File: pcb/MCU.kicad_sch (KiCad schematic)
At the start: 14 parts, among them SW1 SW_Push, SW1 SW_SPDT, U1 STM32F071RBTx, Y1 TG2520SMN_16.0000M-MCGNNM0

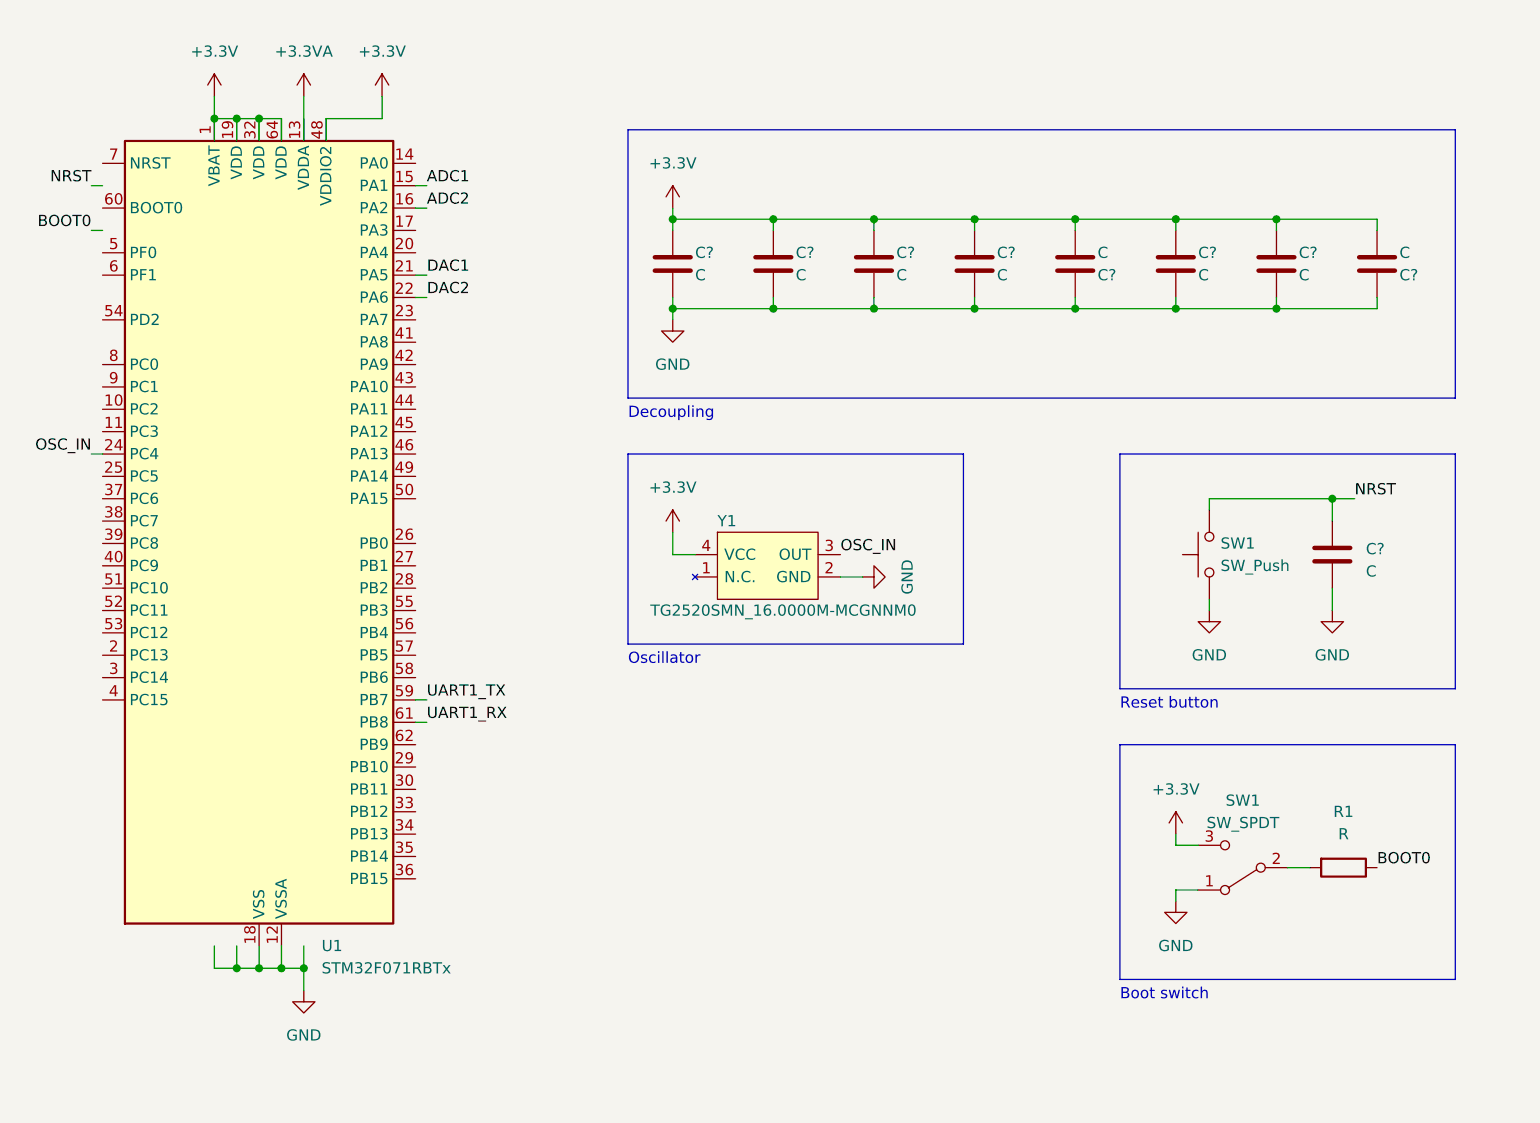
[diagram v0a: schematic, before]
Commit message: Completed schematic oranization and components connection
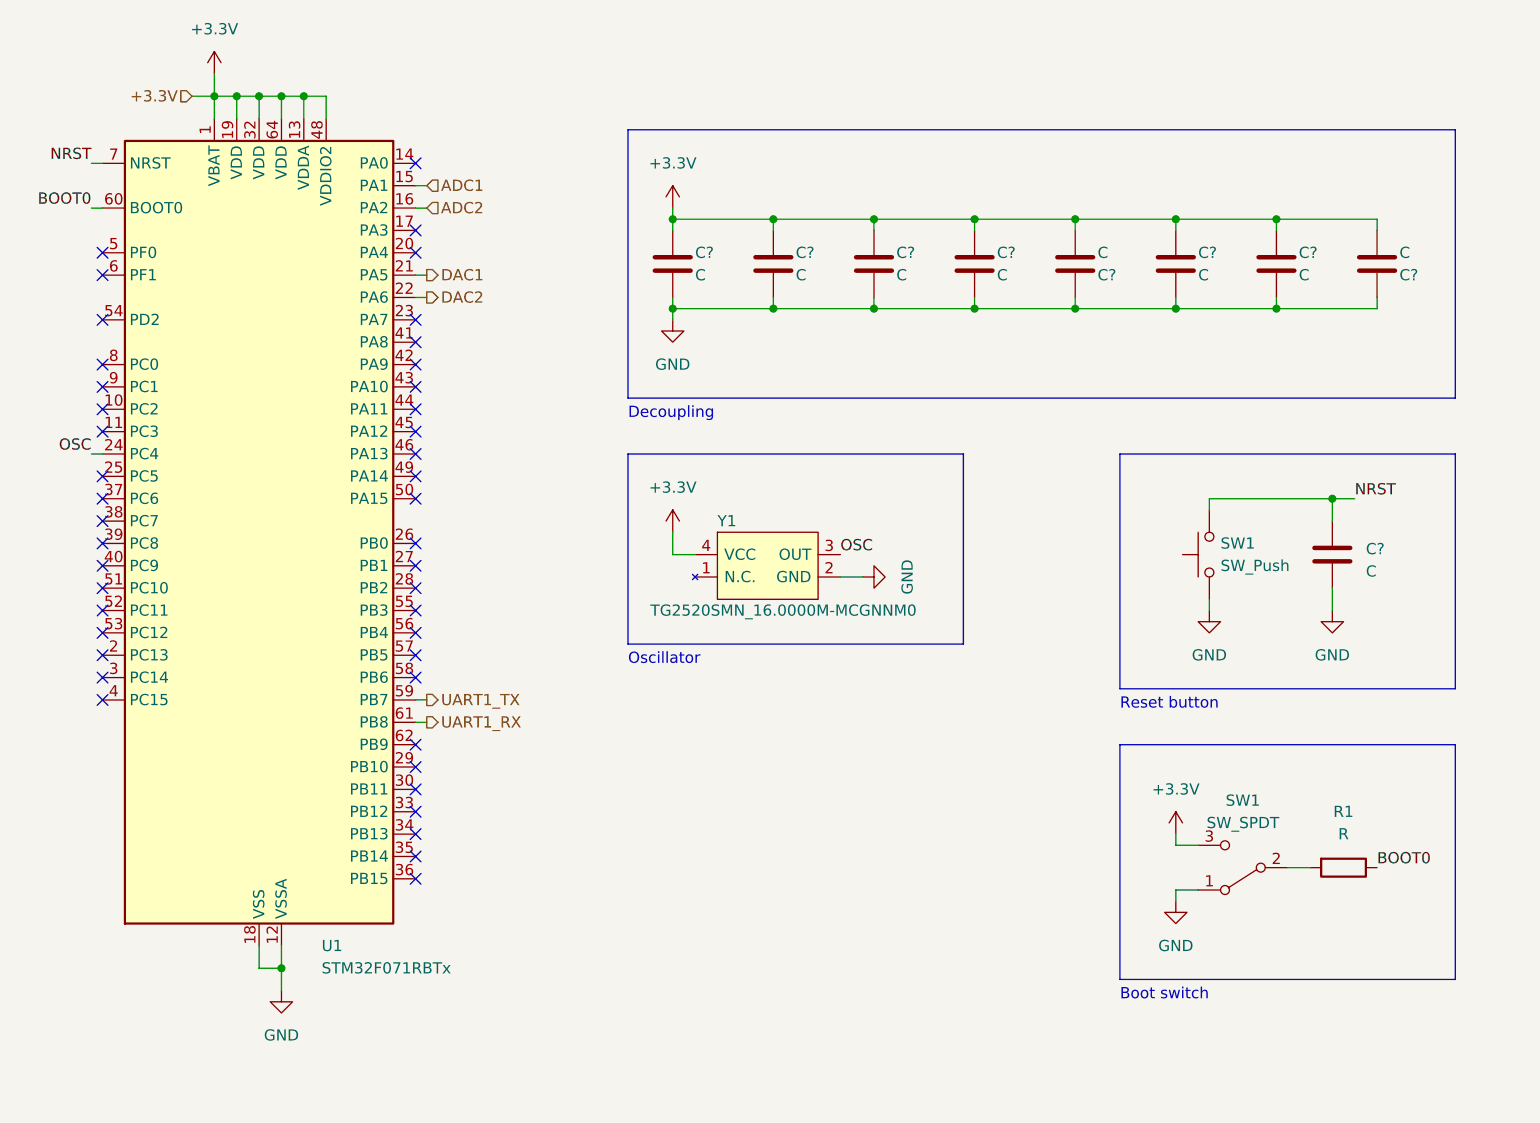
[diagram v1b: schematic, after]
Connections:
- net +3.3V: now also U1.13 (VDDA)
- net BOOT0: now also U1.60 (BOOT0)
- net NRST: now also U1.7 (NRST)
- net OSC_IN renamed OSC
- no-connect marks 0 -> 44

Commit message: Added micro SD and RGB led to schematic. Also added components part numbers
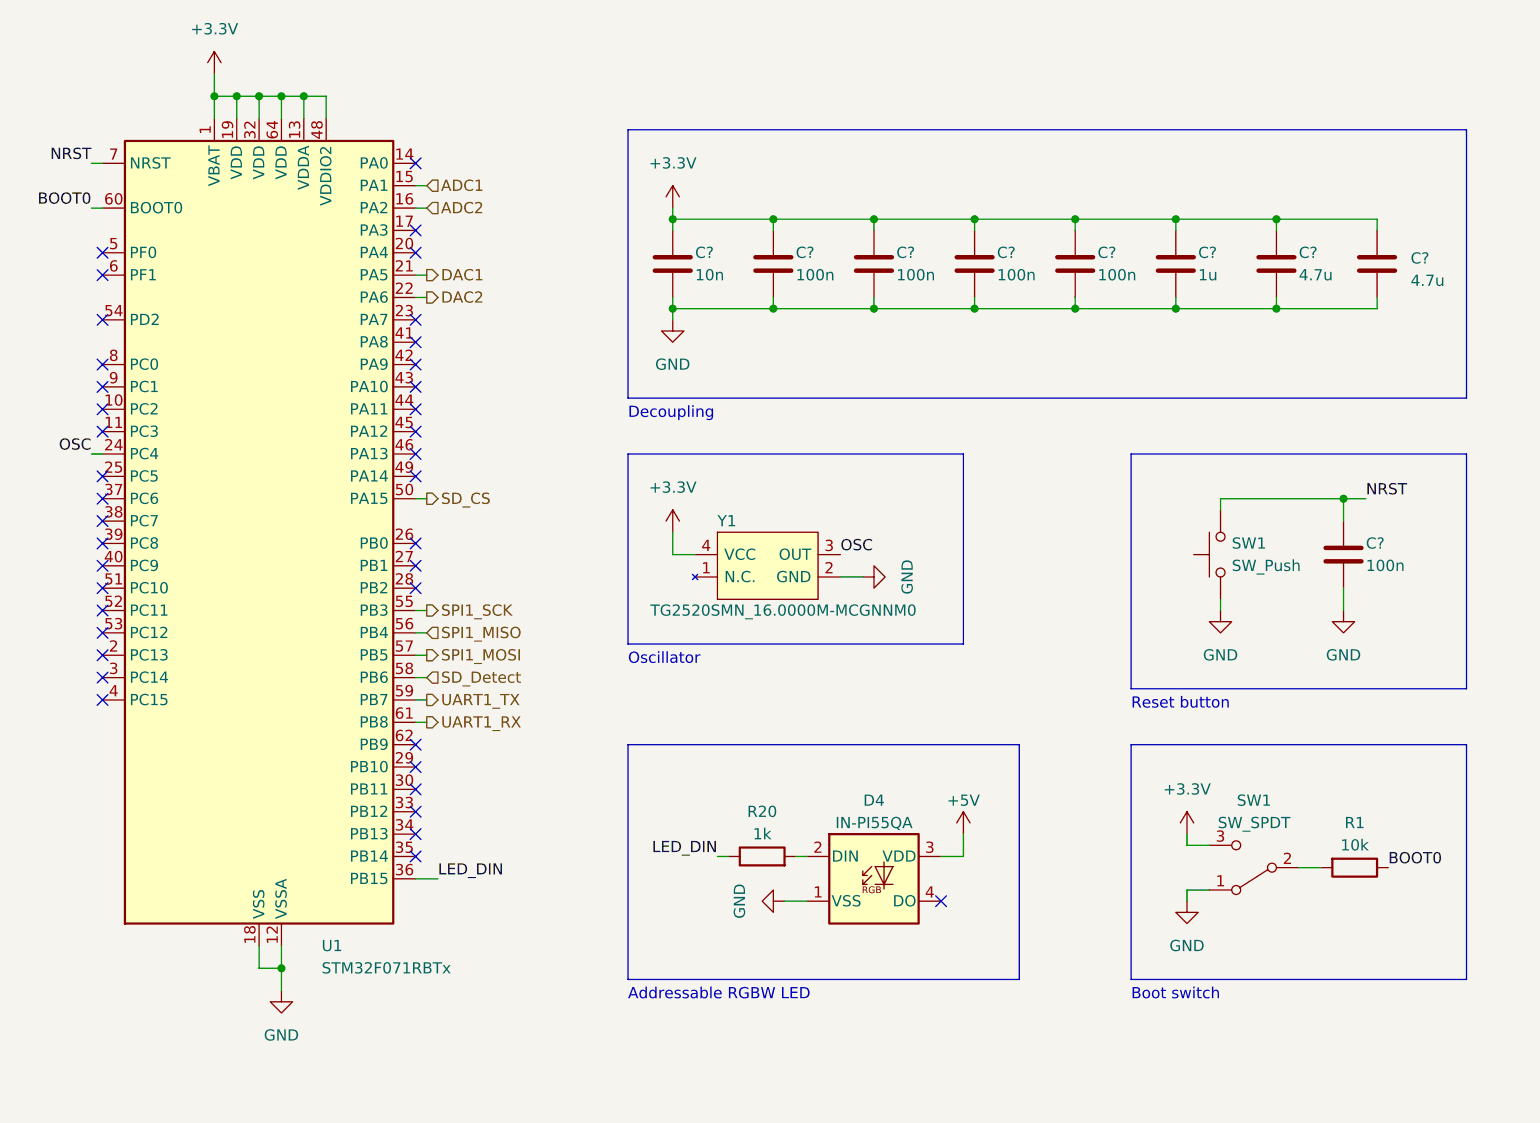
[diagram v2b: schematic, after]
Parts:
- removed C? (x2): C, Capacitor_SMD:C_0603_1608Metric, symbol Device:C
- added C?: 4.7u, Capacitor_SMD:C_0603_1608Metric, symbol Device:C
- added C?: 100n, Capacitor_SMD:C_0603_1608Metric, symbol Device:C
- added D4: IN-PI55QA, Signal Generator Components:IN-PI55QA, symbol Signal Generator Components:IN-PI55QA
- added R20: 1k, Resistor_SMD:R_0603_1608Metric, symbol Device:R
- C? (x4): value C -> 100n; PN (none) -> GCM188R71H104KA57J
- C?: value C -> 10n; PN (none) -> GRM1885C1H103JA01J
- C?: value C -> 1u; PN (none) -> GCM188R71C105KA64D
- C?: value C -> 4.7u; PN (none) -> GRM188Z71C475KE21D
- R1: value R -> 10k; PN (none) -> ERJ-3EKF1002V
- U1: PN (none) -> STM32F071RBT6
- Y1: PN (none) -> TG2520SMN_16.0000M-MCGNNM0
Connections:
- net +3.3V: now also C?.1, C?.1; no longer C?.2
- net GND: now also C?.2, C?.2, C?.2, D4.1 (VSS); no longer C?.1
- net NRST: now also C?.1
- net LED_DIN: now reaches U1.36 (PB15)
- net LED_DIN: now also R20.1
- net SD_CS: now reaches U1.50 (PA15)
- net SPI1_SCK: now reaches U1.55 (PB3)
- net SPI1_MISO: now reaches U1.56 (PB4)
- net SPI1_MOSI: now reaches U1.57 (PB5)
- net SD_Detect: now reaches U1.58 (PB6)
- new net: D4.2 (DIN), R20.2
- new net +5V: D4.3 (VDD)
- no-connect marks 44 -> 39
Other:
- note added: "Addressable RGBW LED"
- moved on the sheet: R1, SW1

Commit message: Completed schematic and tried some simulations
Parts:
- renumbered D4 to D3, R20 to R17
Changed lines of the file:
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@@
   (title_block
     (title "Microcontroller Unit")
+    (date "2023-01-16")
+    (rev "0")
   )
   (junction (at 96.52 152.4) (diameter 0) (color 0 0 0 0)
@@
         )
         (path "/f6255c48-6253-4c69-a6db-1ceaf4eff04d/fadc918d-eb15-47ed-9103-62412ffd5e96"
-          (reference "R17") (unit 1)
+          (reference "R18") (unit 1)
         )
       )
@@
   (symbol (lib_id "Device:R") (at 151.13 139.7 90) (unit 1)
     (in_bom yes) (on_board yes) (dnp no) (fields_autoplaced)
-    (property "Reference" "R20" (at 151.13 134.62 90)
+    (property "Reference" "R17" (at 151.13 134.62 90)
       (effects (font (size 1.27 1.27)))
     )
@@
       (project "Signal Generator"
         (path "/f6255c48-6253-4c69-a6db-1ceaf4eff04d/fadc918d-eb15-47ed-9103-62412ffd5e96"
-          (reference "R20") (unit 1)
+          (reference "R17") (unit 1)
         )
       )
@@
   (symbol (lib_id "Signal Generator Components:IN-PI55QA") (at 163.83 142.24 0) (unit 1)
     (in_bom yes) (on_board yes) (dnp no) (fields_autoplaced)
-    (property "Reference" "D4" (at 163.83 133.35 0)
+    (property "Reference" "D3" (at 163.83 133.35 0)
       (effects (font (size 1.27 1.27)))
     )
@@
       (project "Signal Generator"
         (path "/f6255c48-6253-4c69-a6db-1ceaf4eff04d/fadc918d-eb15-47ed-9103-62412ffd5e96"
-          (reference "D4") (unit 1)
-        )
-      )
+          (reference "D3") (unit 1)
+        )
+      )

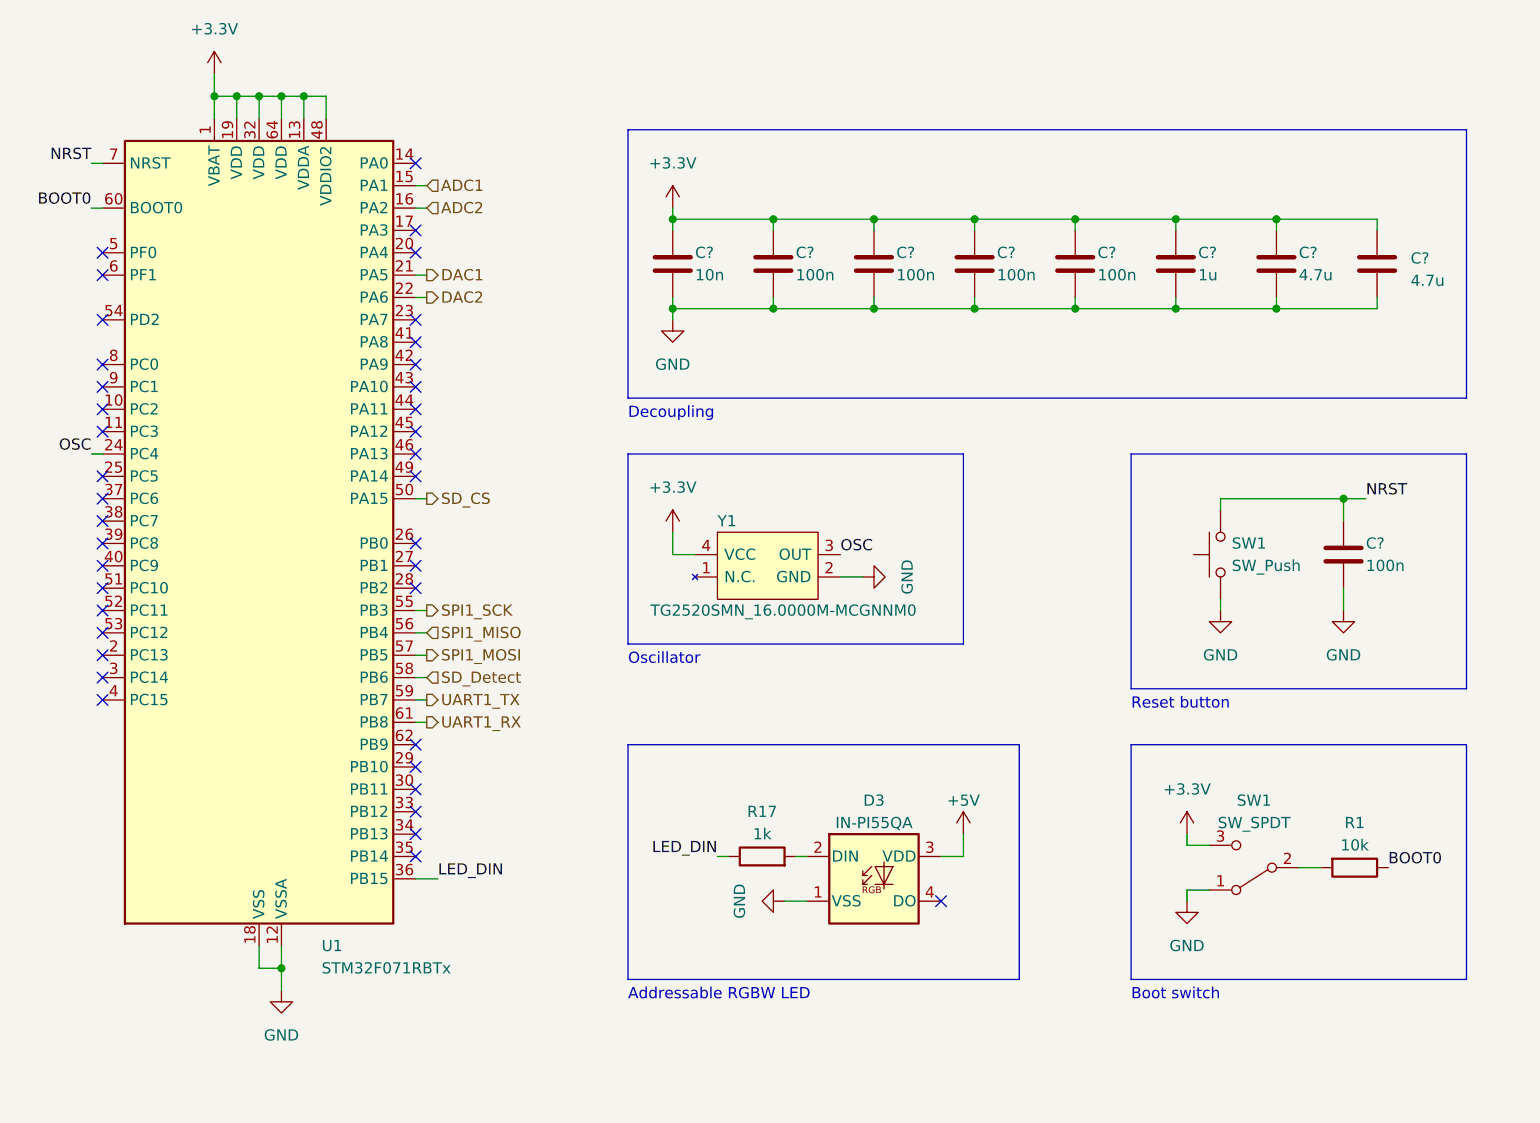
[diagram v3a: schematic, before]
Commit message: Added ST-Link connector to schematic
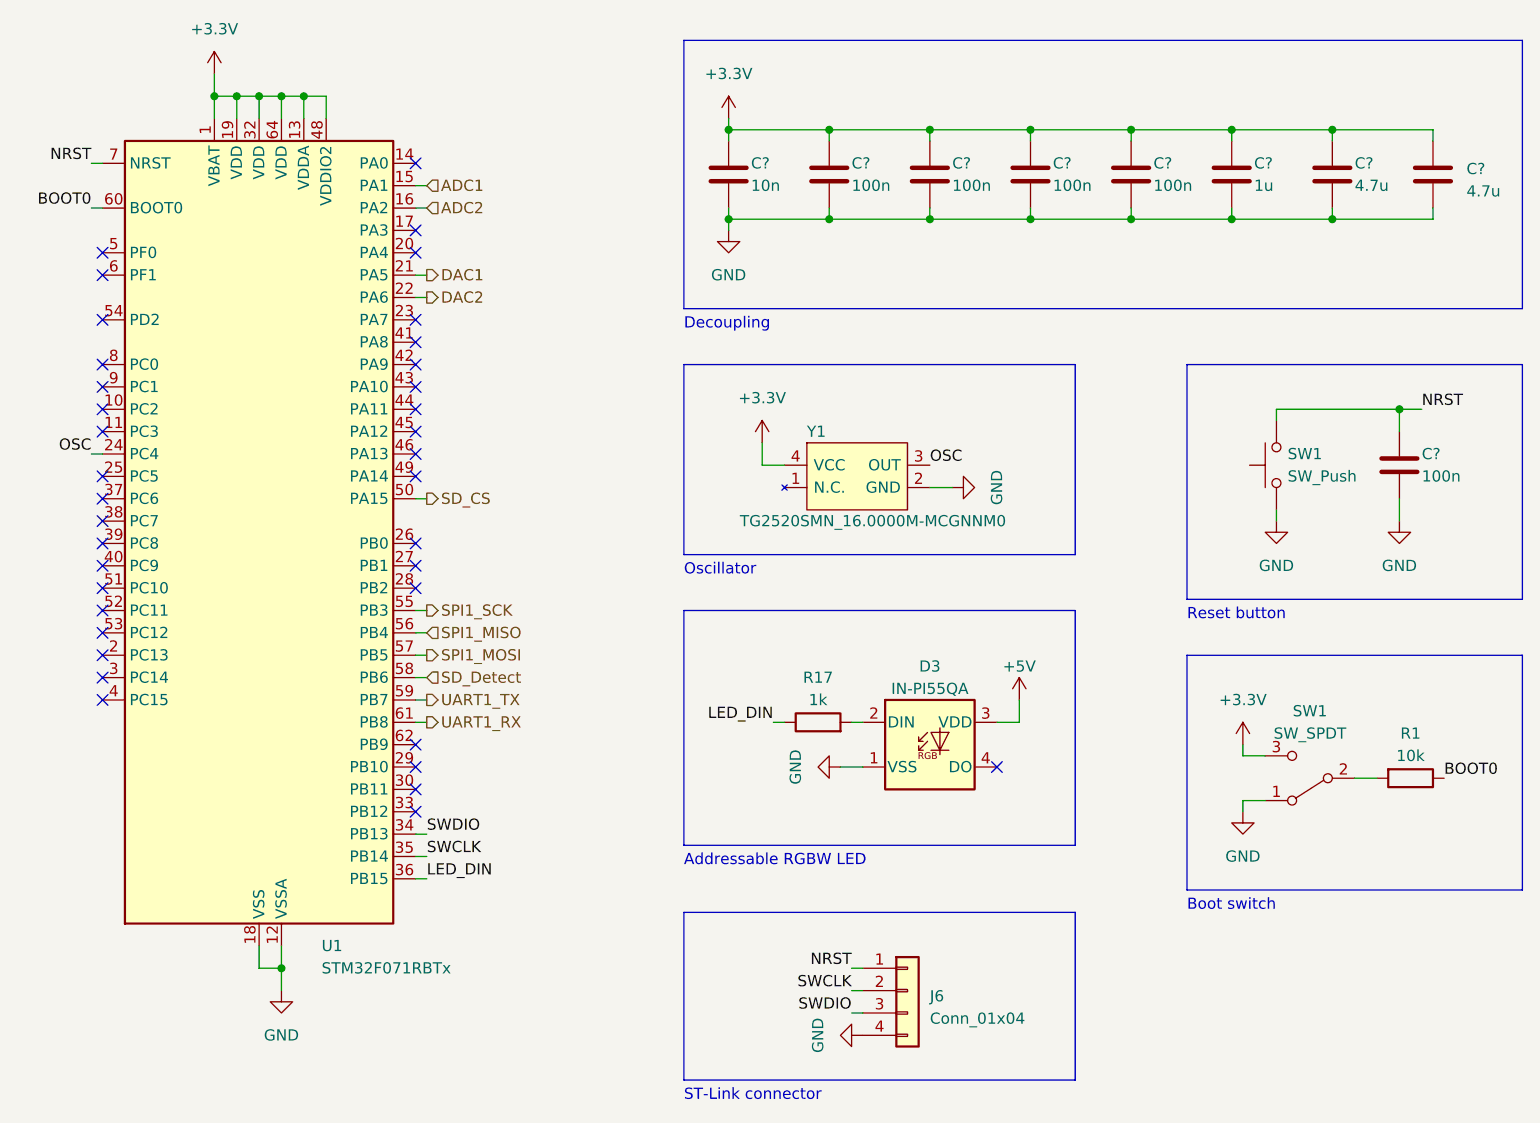
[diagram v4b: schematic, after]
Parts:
- added J6: Conn_01x04, Connector_PinHeader_2.54mm:PinHeader_1x04_P2.54mm_Horizontal, symbol Connector_Generic:Conn_01x04
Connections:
- net GND: now also J6.4 (Pin_4)
- net NRST: now also J6.1 (Pin_1)
- net SWDIO: now reaches U1.34 (PB13)
- net SWDIO: now also J6.3 (Pin_3)
- net SWCLK: now reaches U1.35 (PB14)
- net SWCLK: now also J6.2 (Pin_2)
- no-connect marks 39 -> 37
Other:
- note added: "ST-Link connector"
- moved on the sheet: C?, D3, R1, R17, SW1, Y1

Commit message: Updated PCB
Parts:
- removed C?: 4.7u, Capacitor_SMD:C_0603_1608Metric, symbol Device:C
- removed U1: STM32F071RBTx, Package_QFP:LQFP-64_10x10mm_P0.5mm, symbol MCU_ST_STM32F0:STM32F071RBTx
- added U3: STM32F103RBTx, Package_QFP:LQFP-64_10x10mm_P0.5mm, symbol MCU_ST_STM32F1:STM32F103RBTx
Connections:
- net +3.3V: now also U3.1 (VBAT), U3.13 (VDDA), U3.19 (VDD), U3.32 (VDD), U3.48 (VDD), U3.64 (VDD)
- net ADC1: now also U3.15 (PA1)
- net ADC2: now also U3.16 (PA2)
- net BOOT0: now also U3.60 (BOOT0)
- net DAC1: now also U3.21 (PA5)
- net DAC2: now also U3.22 (PA6)
- net GND: now also U3.12 (VSSA), U3.18 (VSS), U3.31 (VSS), U3.47 (VSS), U3.63 (VSS)
- net LED_DIN: now also U3.36 (PB15)
- net NRST: now also U3.7 (NRST)
- net OSC: now also U3.25 (PC5)
- net SD_CS: now also U3.50 (PA15)
- net SD_Detect: now also U3.58 (PB6)
- net SPI1_MISO: now also U3.56 (PB4)
- net SPI1_MOSI: now also U3.57 (PB5)
- net SPI1_SCK: now also U3.55 (PB3)
- net SWCLK: now also U3.35 (PB14)
- net SWDIO: now also U3.34 (PB13)
- net UART1_RX: now also U3.61 (PB8)
- net UART1_TX: now also U3.59 (PB7)
